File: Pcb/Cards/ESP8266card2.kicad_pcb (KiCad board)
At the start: 2 copper layers, 41.9 x 36.8 mm, 17 parts, among them P1 , P2 , P3 CA6_CONN_01X10, U1 ESP-12E/F

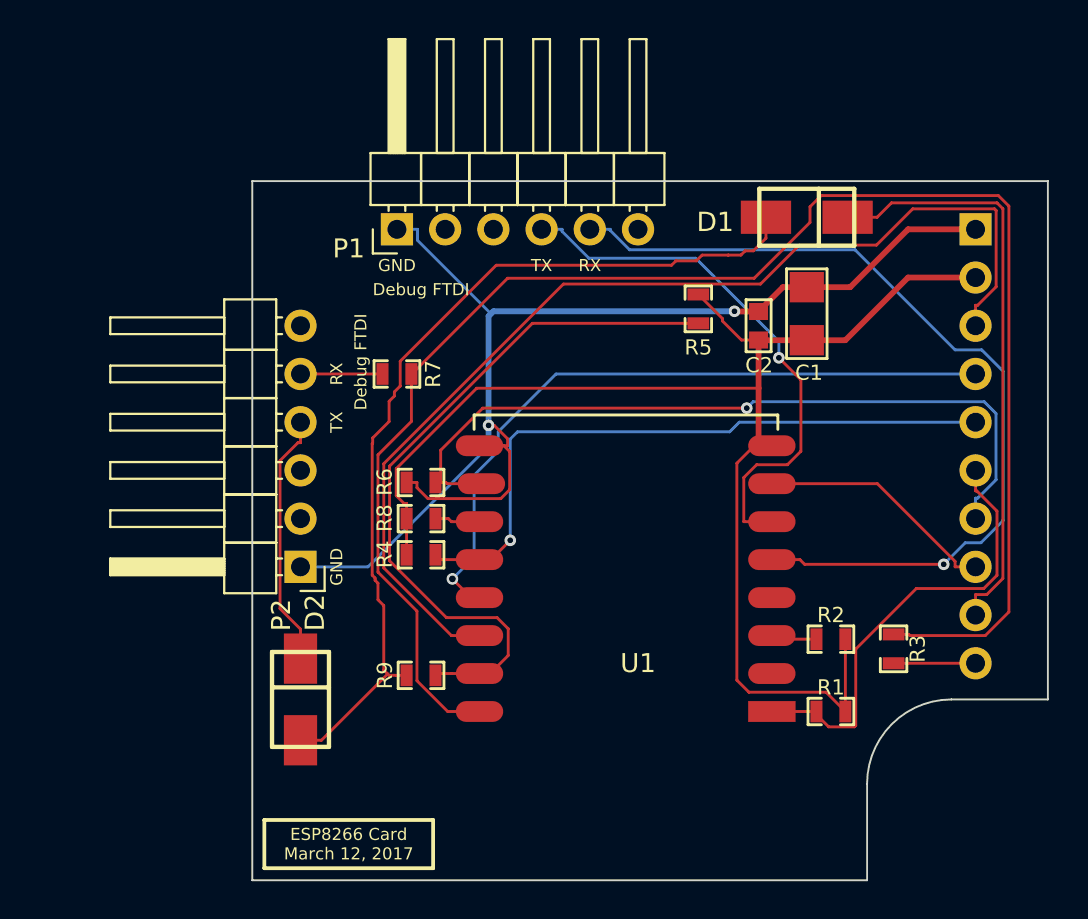
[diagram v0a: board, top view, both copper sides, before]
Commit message: Temp commit to check and update dimensions between CA6 board and connection card
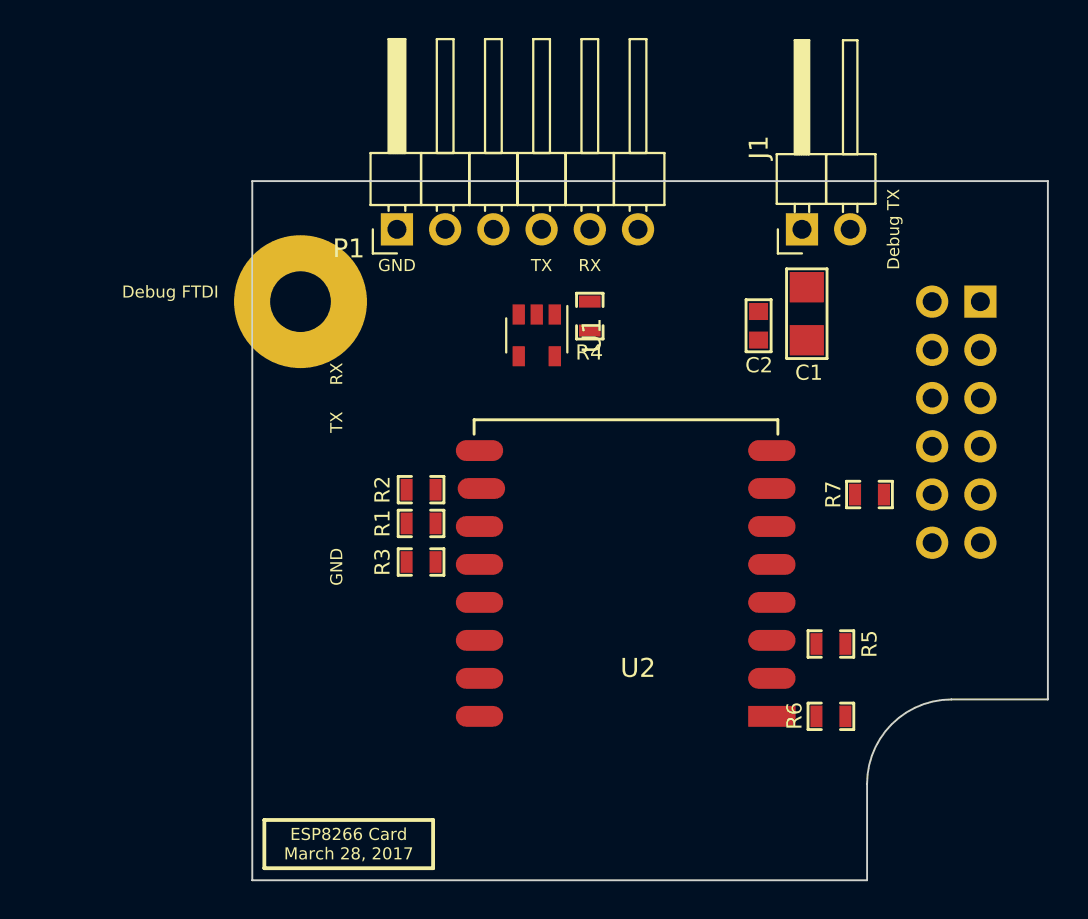
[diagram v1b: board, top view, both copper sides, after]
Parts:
- removed D1, D2: diode_schottky_20V_1A, CA6:DO-214AC(SMA)
- removed P2: , Pin_Headers:Pin_Header_Angled_1x06_Pitch2.54mm
- removed P3: CA6_CONN_01X10, Pin_Header_Straight_1x10_Pitch2.54mm
- removed R8: 10K, CA6:SM0603_Resistor
- removed R9: 1K, CA6:SM0603_Resistor
- added J1: CONN_01X02, Pin_Headers:Pin_Header_Angled_1x02_Pitch2.54mm, F.Cu at (185.2, 101.6)
- added J2: CONN_02X06, Pin_Headers:Pin_Header_Straight_2x06_Pitch2.54mm, B.Cu at (194.6, 105.4)
- added U2: ESP-12E/F, CA6:ESP-12E-F-no-bottom-pads, F.Cu at (182.9, 127.3)
- added X3: HOLE, CA6:HOLE_3.0mm, F.Cu at (158.8, 105.4)
- C1: value 10uF -> .1uF
- C2: value .1uF -> 10uF
- P1: value (none) -> ESP-Programming-FTDI
- R3: value 1K -> 10K
- R4: value 10K -> 1K
- U1: value ESP-12E/F -> SN74AHC1G08; footprint CA6:ESP-12E-F-no-bottom-pads -> TO_SOT_Packages_SMD:SOT-23-5
- moved R7 25.7 mm to (188.7, 115.6), turned to 180 degrees
- moved R3 25.3 mm to (165.1, 119.1), turned to 0 degrees
- moved R6 24.9 mm to (186.7, 127.3)
- moved R1 23.8 mm to (165.1, 117.1)
- moved U1 23.0 mm to (171.2, 107.2), turned to 270 degrees
- moved R2 23.0 mm to (165.1, 115.3)
- moved R5 19.0 mm to (186.7, 123.4), turned to 0 degrees
- moved R4 15.4 mm to (174.0, 106.2), turned to 90 degrees
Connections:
- P1 pad 4: /Debug-RX -> Net-(P1-Pad4)
- P1 pad 5: /Debug-TX -> Net-(P1-Pad5)
- R1 pad 1: /CC_RESET -> 3V3
- R1 pad 2: 3V3 -> /Debug-TX
- R2 pad 1: Net-(R2-Pad1) -> GND
- R2 pad 2: 3V3 -> /CC_CTS
- R3 pad 1: /ESP_TX -> 3V3
- R3 pad 2: /CC_RX -> /CC_PROG
- R4 pad 1: 3V3 -> /ESP_TX
- R4 pad 2: /CC_PROG -> Net-(P1-Pad5)
- R5 pad 1: 3V3 -> Net-(R5-Pad1)
- R5 pad 2: /ESP_RX -> 3V3
- R6 pad 1: GND -> /CC_RESET
- R6 pad 2: /CC_CTS -> 3V3
- R7 pad 1: Net-(P2-Pad5) -> /CC_RX
- U1 pad 1: /CC_RESET -> /CC_TX
- U1 pad 2: Net-(U1-Pad2) -> Net-(P1-Pad4)
- U1 pad 3: Net-(R2-Pad1) -> /ESP_RX
- U1 pad 4: Net-(U1-Pad4) -> (no net)
- U1 pad 5: /Debug-TX -> (no net)
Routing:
- net /ESP_TX: track 86.5 -> 0.00 mm
- net 3V3: track 71.5 -> 0.00 mm
- net GND: track 65.1 -> 0.00 mm, vias 2 -> 0
- net /R-LED: track 57.2 -> 0.00 mm
- net Net-(D1-Pad2): track 47.5 -> 0.00 mm
- net /Debug-TX: track 46.7 -> 0.00 mm, vias 1 -> 0
- net /CC_CTS: track 41.4 -> 0.00 mm, vias 1 -> 0
- net /ESP_RX: track 37.9 -> 0.00 mm
- net /G-LED: track 37.7 -> 0.00 mm, vias 1 -> 0
- net /CC_PROG: track 36.3 -> 0.00 mm, vias 1 -> 0
- net /CC_TX: track 31.0 -> 0.00 mm
- net /Debug-RX: track 28.0 -> 0.00 mm, vias 1 -> 0
- net /CC_RESET: track 24.7 -> 0.00 mm
- net Net-(D2-Pad1): track 13.4 -> 0.00 mm
- net /CC_RTS: track 13.4 -> 0.00 mm
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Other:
- board text added: "Debug TX"
- board text added: "ESP8266 Card March 28, 2017"
- board text removed: "ESP8266 Card March 12, 2017"

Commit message: Almost complete ESP8266card2.  Schematic updated with logic gate, removed 1k resistors, updated 2 pull-ups to 4.7k; Board has 2x6 pin connector to CA6 and stability screw.  Board routed, needs some cleanup of labels, etc.  Anyone testing ESP8266 should probably change to this schematic.
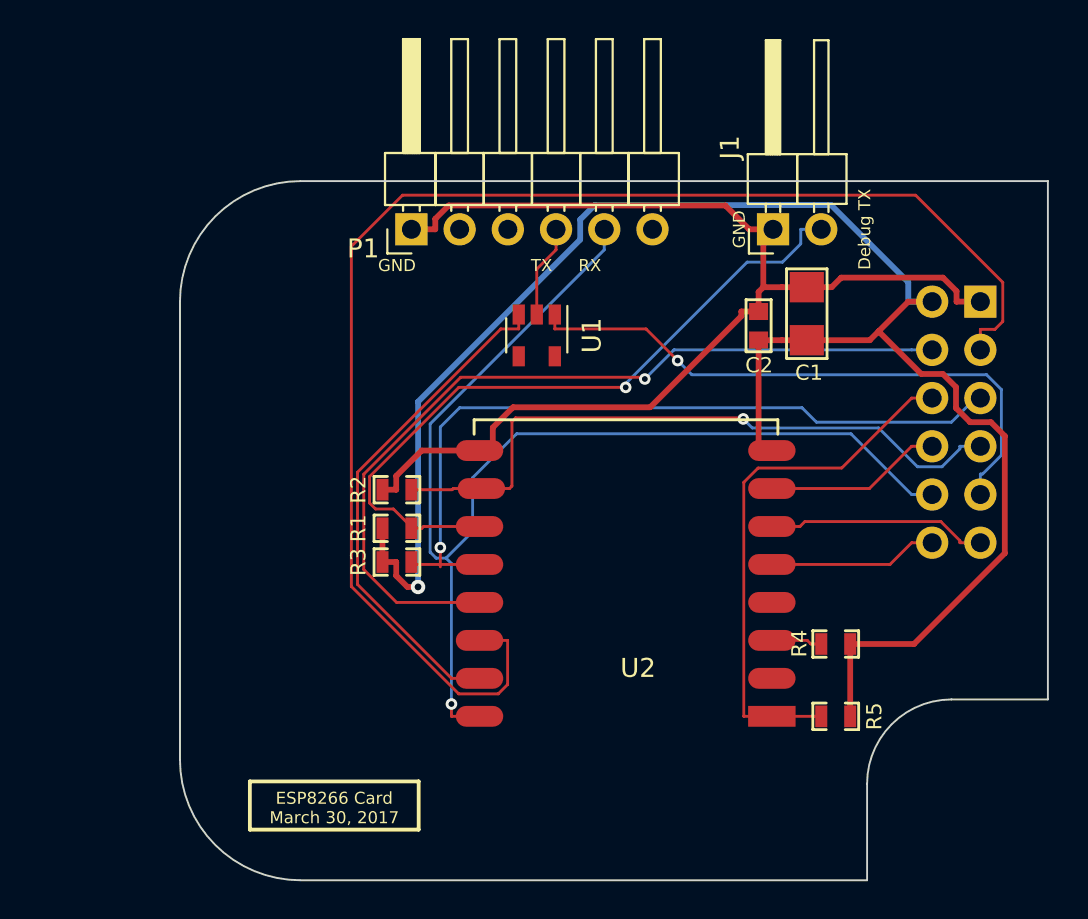
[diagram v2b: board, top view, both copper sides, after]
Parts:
- removed R6: 10K, CA6:SM0603_Resistor
- removed R7: 1K, CA6:SM0603_Resistor
- removed X3: HOLE, CA6:HOLE_3.0mm
- R3, R5: value 10K -> 4.7k
- R4: value 1K -> 10K
- moved R4 21.6 mm to (186.9, 123.4), turned to 0 degrees
- moved R5 3.82 mm to (186.9, 127.3)
- moved J1 1.52 mm to (183.6, 101.6)
- moved R1 1.30 mm to (163.8, 117.3)
- moved R2 1.27 mm to (163.8, 115.3)
- moved R3 1.27 mm to (163.8, 119.1)
- moved P1 0.76 mm to (164.6, 101.6)
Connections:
- P1 pad 5: Net-(P1-Pad5) -> /CC_RX
- R4 pad 1: /ESP_TX -> Net-(R4-Pad1)
- R4 pad 2: Net-(P1-Pad5) -> 3V3
- R5 pad 1: Net-(R5-Pad1) -> /CC_RESET
- U2 pad 16: /ESP_TX -> /CC_RX
- U2 pad 3: Net-(R5-Pad1) -> Net-(R4-Pad1)
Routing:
- net 3V3: track 0.00 -> 94.6 mm, vias 0 -> 1
- net /CC_R_LED: track 0.00 -> 73.6 mm
- net /CC_RX: track 0.00 -> 63.7 mm, vias 0 -> 1
- net GND: track 0.00 -> 62.3 mm
- net /CC_G_LED: track 0.00 -> 45.3 mm, vias 0 -> 1
- net /CC_PROG: track 0.00 -> 41.4 mm, vias 0 -> 1
- net /Debug-TX: track 0.00 -> 38.3 mm, vias 0 -> 1
- net /CC_CTS: track 0.00 -> 35.1 mm, vias 0 -> 1
- net /CC_TX: track 0.00 -> 31.7 mm, vias 0 -> 1
- net /CC_RESET: track 0.00 -> 28.2 mm
- net /ESP_RX: track 0.00 -> 27.5 mm
- net /CC_EXT1: track 0.00 -> 12.3 mm
- net /CC_RTS: track 0.00 -> 10.1 mm
- net /CC_EXT0: track 0.00 -> 9.62 mm
- net Net-(P1-Pad4): track 0.00 -> 4.91 mm
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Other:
- board size 41.9 x 36.8 mm -> 45.7 x 36.8 mm
- board text added: "ESP8266 Card March 30, 2017"
- board text added: "notch for screw on CA6 brd"
- board text removed: "Debug FTDI"
- board text removed: "ESP8266 Card March 28, 2017"
- board text removed: "hole or notch for screw"

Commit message: Corrected ESP8266card2 for AND gate pins, routing and text.  Added first version of nRF52card.  Put all components in CA6.lib and CA6.pretty   Still needs checking expecially for text.
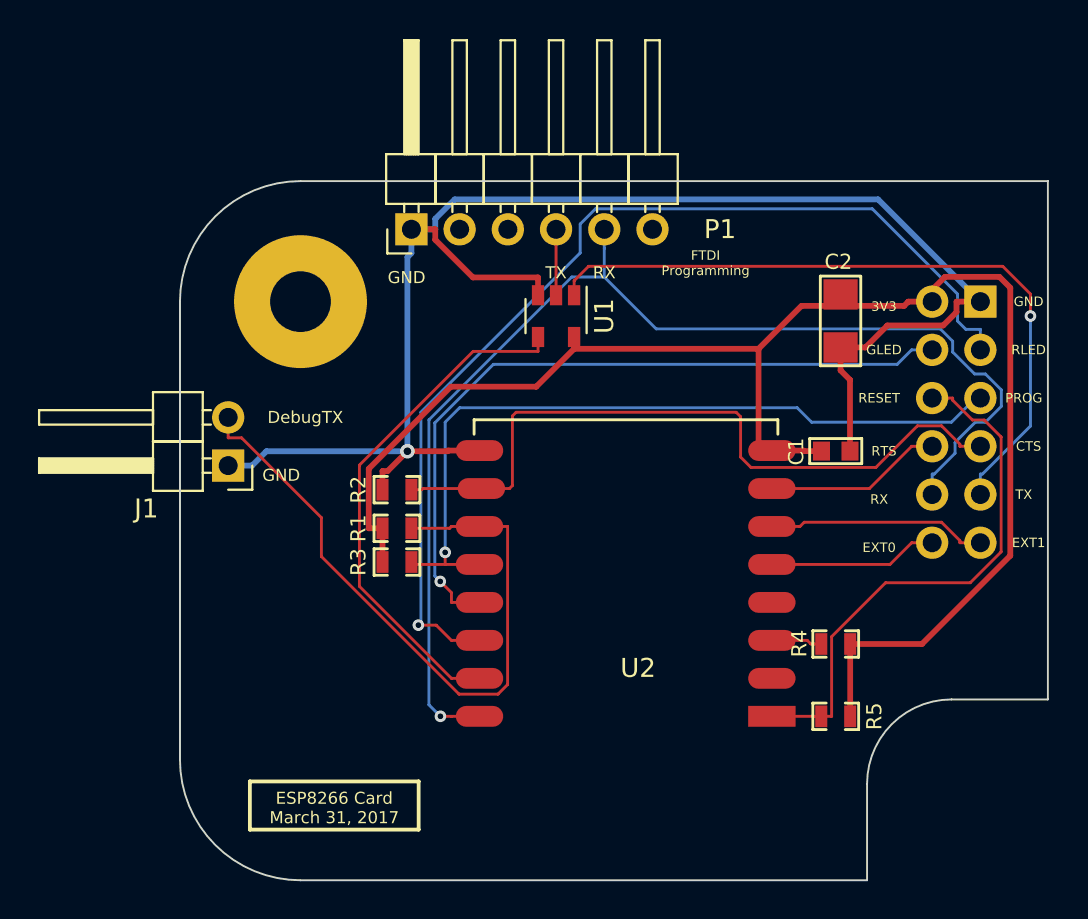
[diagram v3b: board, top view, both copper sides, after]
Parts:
- added X1: HOLE, CA6:HOLE_3.0mm, F.Cu at (158.8, 105.4)
- C1: footprint CA6:c_1206 -> CA6:c_0603
- C2: footprint CA6:c_0603 -> CA6:c_1206
- J1: value CONN_01X02 -> Debug_TX; footprint Pin_Headers:Pin_Header_Angled_1x02_Pitch2.54mm -> CA6:Pin_Header_Angled_1x02_Pitch2.54mm
- J2: value CONN_02X06 -> CA6_02X06; footprint Pin_Headers:Pin_Header_Straight_2x06_Pitch2.54mm -> CA6:Pin_Header_Straight_2x06_Pitch2.54mm
- P1: footprint Pin_Headers:Pin_Header_Angled_1x06_Pitch2.54mm -> CA6:Pin_Header_Angled_1x06_Pitch2.54mm
- U1: footprint TO_SOT_Packages_SMD:SOT-23-5 -> CA6:SOT-23-5_GATE
- moved J1 31.3 mm to (154.9, 114.0), turned to 180 degrees
- moved C1 7.40 mm to (186.9, 113.3), turned to 180 degrees
- moved C2 4.33 mm to (187.2, 106.4), turned to 90 degrees
- moved U1 1.44 mm to (172.2, 106.2)
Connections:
- net Net-(P1-Pad4) renamed /FTDI_TX
- U1 pad 3: /ESP_RX -> GND
- U1 pad 4: (no net) -> /ESP_RX
- U1 pad 5: (no net) -> 3V3
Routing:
- net GND: track 62.3 -> 85.3 mm, vias 0 -> 1
- net /CC_R_LED: track 73.6 -> 54.9 mm, vias 0 -> 1
- net 3V3: track 94.6 -> 82.7 mm, vias 1 -> 0
- net /CC_TX: track 31.7 -> 37.4 mm
- net /CC_G_LED: track 45.3 -> 39.8 mm
- net /CC_CTS: track 35.1 -> 37.7 mm, vias 1 -> 0
- net /Debug-TX: track 38.3 -> 36.2 mm, vias 1 -> 0
- net /FTDI_TX: track 4.91 -> 3.47 mm
- net /CC_RESET: track 28.2 -> 29.4 mm
- net /CC_RX: track 63.7 -> 64.6 mm
- net /ESP_RX: track 27.5 -> 28.1 mm
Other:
- board text added: "DebugTX"
- board text added: "ESP8266 Card March 31, 2017"
- board text added: "EXT0"
- board text added: "EXT1"
- board text added: "FTDI Programming"
- board text added: "GLED"
- board text added: "RLED"
- board text removed: "Debug TX"
- board text removed: "ESP8266 Card March 30, 2017"
- board text removed: "G-LED"
- board text removed: "R-LED"
